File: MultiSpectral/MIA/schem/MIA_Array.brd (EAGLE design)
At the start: 99 x 99 mm, 52 parts

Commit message: updated schematic boarders
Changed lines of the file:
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@@
 <dimension x1="0" y1="0" x2="100" y2="0.25" x3="50.032434375" y3="-12.84929375" textsize="1.778" layer="1"/>
 <dimension x1="0" y1="0" x2="0" y2="100" x3="-10.75" y3="50" textsize="1.778" layer="1" dtype="diameter"/>
-<wire x1="0.5" y1="47.25" x2="47.75" y2="0.5" width="1.016" layer="46" curve="-89.847631"/>
-<wire x1="0.5" y1="99.5" x2="99.5" y2="0.5" width="1.016" layer="46" curve="-89.641185"/>
+<wire x1="0.5" y1="47.25" x2="47.75" y2="0.5" width="1.016" layer="20" curve="-89.847631"/>
+<wire x1="0.5" y1="99.5" x2="99.5" y2="0.5" width="1.016" layer="20" curve="-89.641185"/>
+<wire x1="47.75" y1="0.5" x2="99.5" y2="0.5" width="1.016" layer="20"/>
+<wire x1="0.5" y1="99.5" x2="0.5" y2="47.25" width="1.016" layer="20"/>
 </plain>
 <attributes>

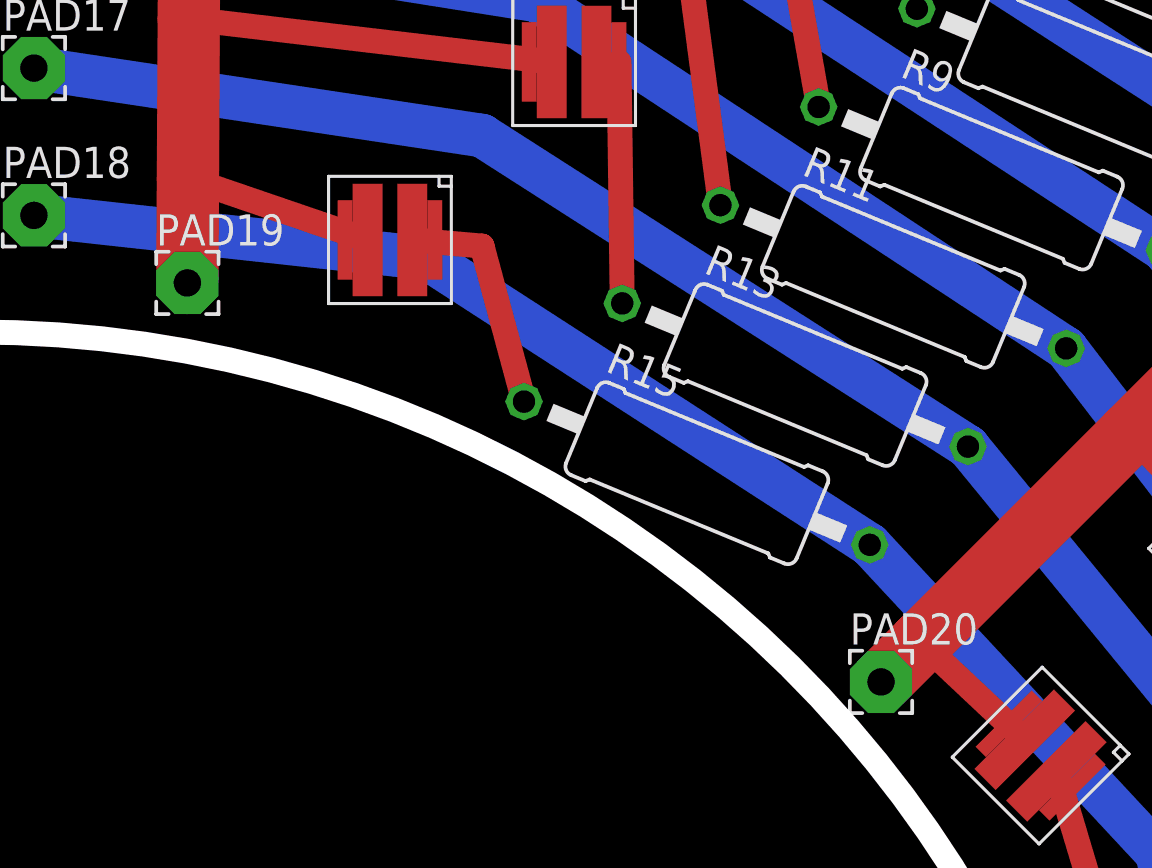
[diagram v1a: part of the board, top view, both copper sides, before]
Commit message: Moved pad20 closer to edge to avoid conflict with center anode trace
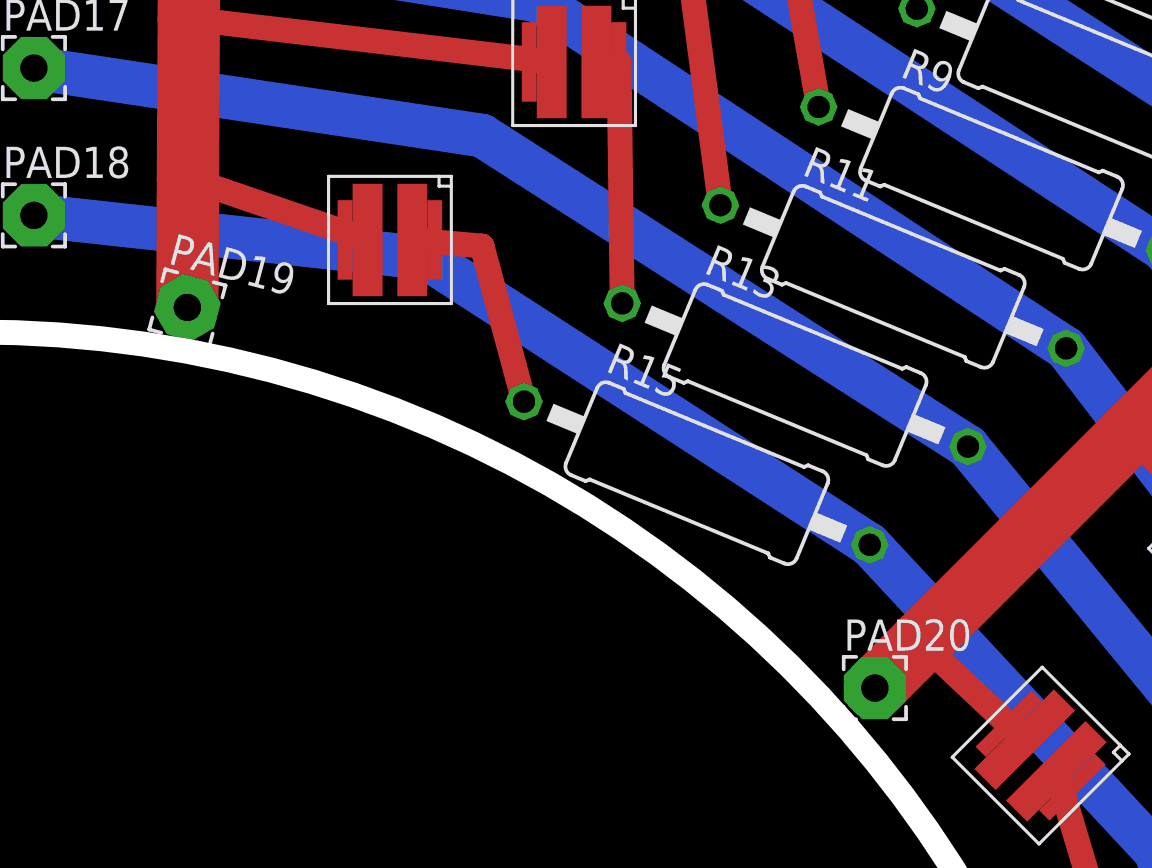
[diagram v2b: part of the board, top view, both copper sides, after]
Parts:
- moved PAD19 1.00 mm to (9.25, 48.2), turned to 345 degrees
- moved PAD20 0.35 mm to (37.2, 32.8)
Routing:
- net N$11: track 180.6 -> 181.6 mm
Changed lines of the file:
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@@
 <element name="PAD17" library="wirepad" package="2,54/1,1" value="" x="3" y="58"/>
 <element name="PAD18" library="wirepad" package="2,54/1,1" value="" x="3" y="52"/>
-<element name="PAD19" library="wirepad" package="2,54/1,1" value="" x="9.25" y="49.25"/>
-<element name="PAD20" library="wirepad" package="2,54/1,1" value="" x="37.5" y="33"/>
+<element name="PAD19" library="wirepad" package="2,54/1,1" value="" x="9.25" y="48.25" rot="R345"/>
+<element name="PAD20" library="wirepad" package="2,54/1,1" value="" x="37.25" y="32.75"/>
 </elements>
 <signals>
@@
 <wire x1="51.625" y1="47.125" x2="56.25" y2="51.75" width="2.54" layer="1"/>
 <wire x1="39.125" y1="34.625" x2="47.625" y2="43.125" width="2.54" layer="1"/>
-<wire x1="39.125" y1="34.625" x2="37.5" y2="33" width="2.54" layer="1"/>
+<wire x1="39.125" y1="34.625" x2="37.25" y2="32.75" width="2.54" layer="1"/>
 <wire x1="60.625" y1="56.125" x2="64.875" y2="60.375" width="2.54" layer="1"/>
 <wire x1="60.625" y1="56.125" x2="56.25" y2="51.75" width="2.54" layer="1"/>
@@
 <wire x1="9.484128125" y1="93.500084375" x2="9.47620625" y2="92.002771875" width="2.54" layer="1"/>
 <wire x1="9.484128125" y1="93.500084375" x2="9.5" y2="96.5" width="2.54" layer="1"/>
-<wire x1="9.2725" y1="53.502525" x2="9.25" y2="49.25" width="2.54" layer="1"/>
+<wire x1="9.2725" y1="53.502525" x2="9.25" y2="48.25" width="2.54" layer="1"/>
 <wire x1="16.59" y1="51" x2="9.2725" y2="53.502525" width="1.016" layer="1"/>
 <wire x1="16.84" y1="65.75" x2="9.338634375" y2="66.002175" width="1.016" layer="1"/>
